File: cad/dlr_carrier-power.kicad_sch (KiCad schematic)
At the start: 17 parts, among them U1 AP2112K-3.3, U2 LP5907MFX-3.8, U9 LMR33630ADDA

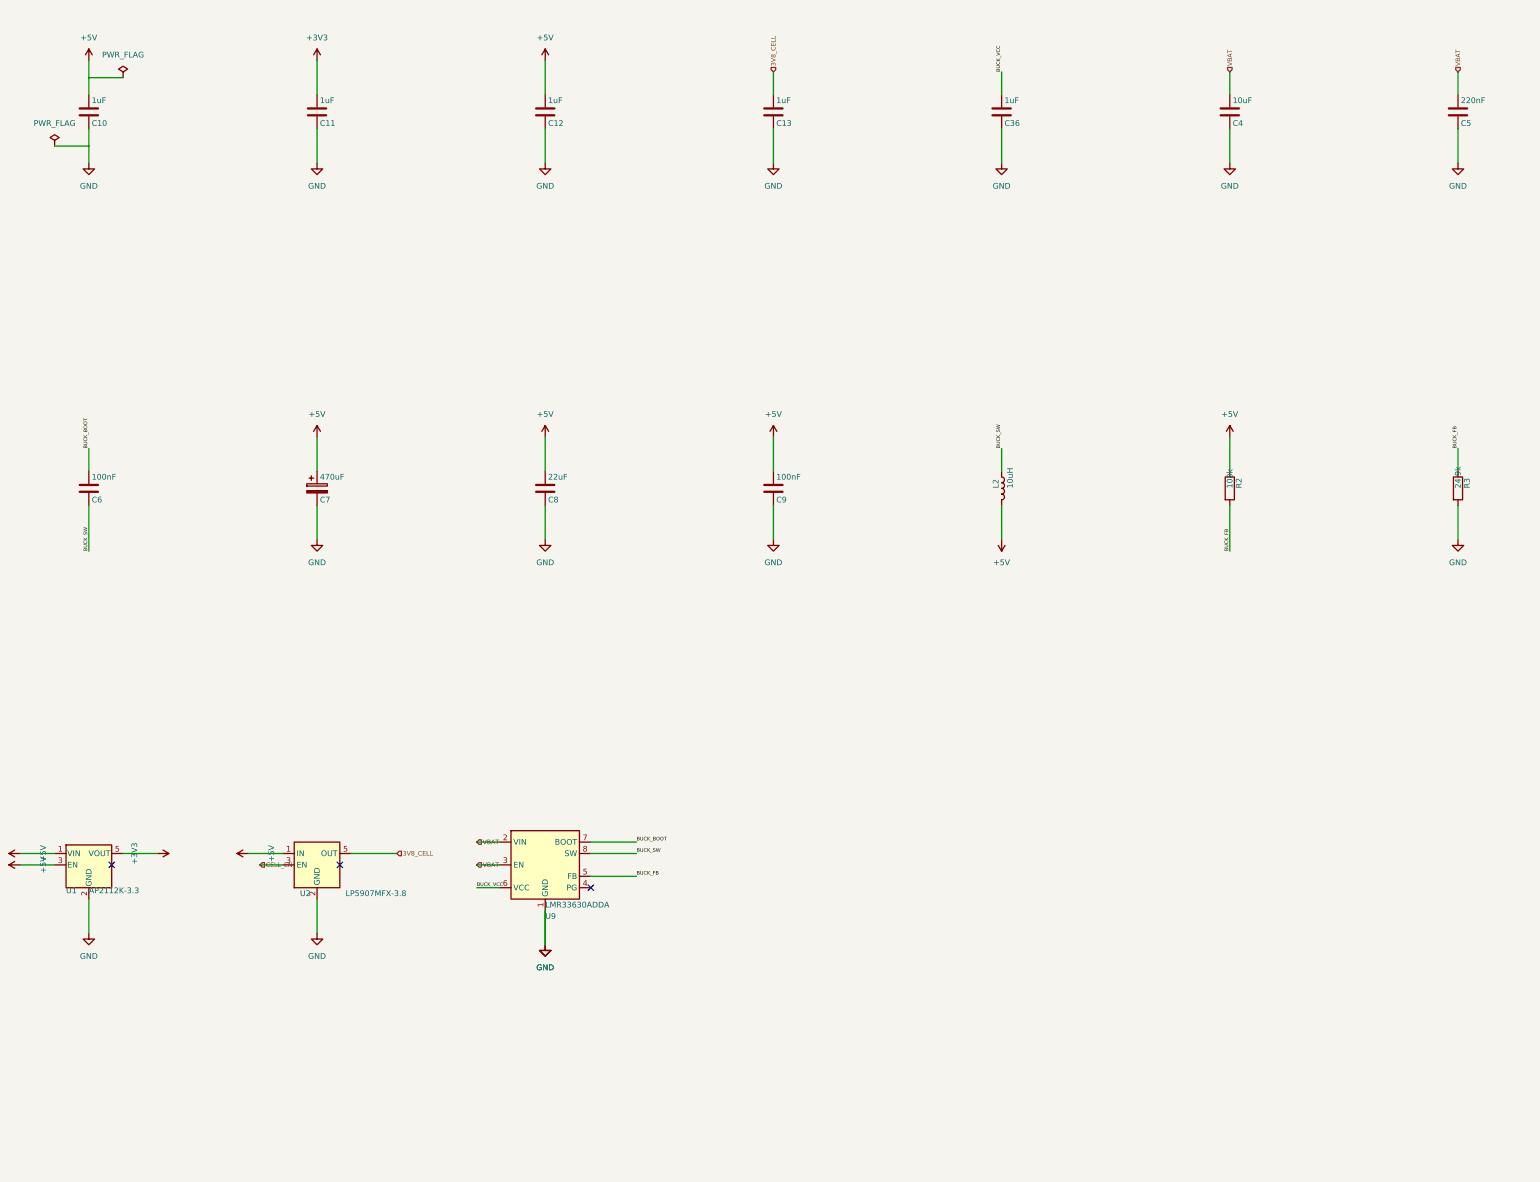
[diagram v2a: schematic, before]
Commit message: 🩺 fix(schematic): match hierarchical label type to the sheet pin
The 117 KiCad 9 errors were a type mismatch, not the hierarchy metadata: every
child hierarchical label was written as `(shape input)` while the root's sheet pins
are bidirectional. KiCad's hier_label_mismatch check compares electrical type as
well as name, so on KiCad 9 every cross-sheet net failed, and the root labels then
read as dangling. KiCad 10 tolerates the mismatch, which is why it passed here.

kicad-sch-api 0.5.6 accepts a shape argument on add_hierarchical_label and ignores
it — the third serialization bug worked around in this generator — so the shape is
rewritten in the saved sheet.

Co-Authored-By: Claude Opus 5 <noreply@anthropic.com>
Claude-Session: https://claude.ai/code/session_011xr7VCL7rkJj2WE2uQF7sF
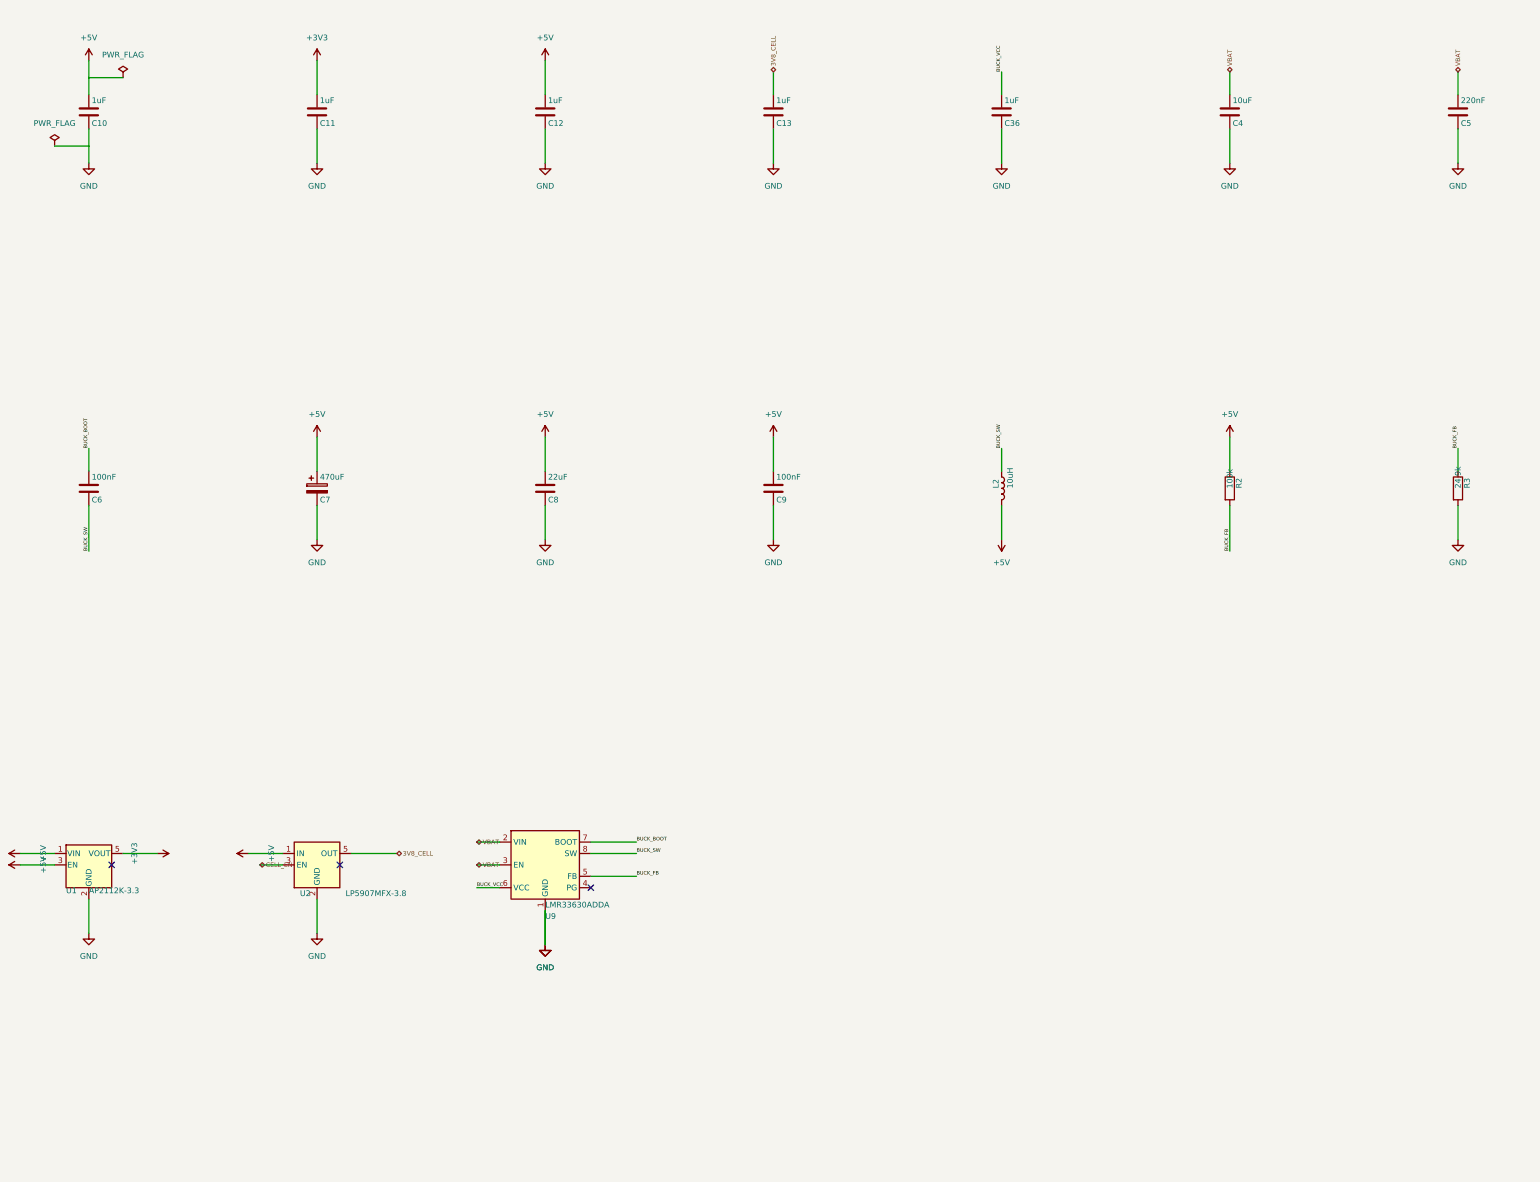
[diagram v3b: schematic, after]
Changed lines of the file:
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@@
 		(instances
 			(project "POWER RAILS"
-				(path "/d7dc1bd5-e6c9-4001-8410-2eaf3fa30cbb"
+				(path "/b92f7d05-346d-4153-84be-6036ac927b56"
 					(reference "C10")
 					(unit 1)
@@
 		(instances
 			(project "POWER RAILS"
-				(path "/d7dc1bd5-e6c9-4001-8410-2eaf3fa30cbb"
+				(path "/b92f7d05-346d-4153-84be-6036ac927b56"
 					(reference "C11")
 					(unit 1)
@@
 		(instances
 			(project "POWER RAILS"
-				(path "/d7dc1bd5-e6c9-4001-8410-2eaf3fa30cbb"
+				(path "/b92f7d05-346d-4153-84be-6036ac927b56"
 					(reference "C12")
 					(unit 1)
@@
 		(instances
 			(project "POWER RAILS"
-				(path "/d7dc1bd5-e6c9-4001-8410-2eaf3fa30cbb"
+				(path "/b92f7d05-346d-4153-84be-6036ac927b56"
 					(reference "C13")
 					(unit 1)
@@
 		(instances
 			(project "POWER RAILS"
-				(path "/d7dc1bd5-e6c9-4001-8410-2eaf3fa30cbb"
+				(path "/b92f7d05-346d-4153-84be-6036ac927b56"
 					(reference "C36")
 					(unit 1)
@@
 		(instances
 			(project "POWER RAILS"
-				(path "/d7dc1bd5-e6c9-4001-8410-2eaf3fa30cbb"
+				(path "/b92f7d05-346d-4153-84be-6036ac927b56"
 					(reference "C4")
 					(unit 1)
@@
 		(instances
 			(project "POWER RAILS"
-				(path "/d7dc1bd5-e6c9-4001-8410-2eaf3fa30cbb"
+				(path "/b92f7d05-346d-4153-84be-6036ac927b56"
 					(reference "C5")
 					(unit 1)
@@
 		(instances
 			(project "POWER RAILS"
-				(path "/d7dc1bd5-e6c9-4001-8410-2eaf3fa30cbb"
+				(path "/b92f7d05-346d-4153-84be-6036ac927b56"
 					(reference "C6")
 					(unit 1)
@@
 		(instances
 			(project "POWER RAILS"
-				(path "/d7dc1bd5-e6c9-4001-8410-2eaf3fa30cbb"
+				(path "/b92f7d05-346d-4153-84be-6036ac927b56"
 					(reference "C7")
 					(unit 1)
@@
 		(instances
 			(project "POWER RAILS"
-				(path "/d7dc1bd5-e6c9-4001-8410-2eaf3fa30cbb"
+				(path "/b92f7d05-346d-4153-84be-6036ac927b56"
 					(reference "C8")
 					(unit 1)
@@
 		(instances
 			(project "POWER RAILS"
-				(path "/d7dc1bd5-e6c9-4001-8410-2eaf3fa30cbb"
+				(path "/b92f7d05-346d-4153-84be-6036ac927b56"
 					(reference "C9")
 					(unit 1)
@@
 		(instances
 			(project "POWER RAILS"
-				(path "/d7dc1bd5-e6c9-4001-8410-2eaf3fa30cbb"
+				(path "/b92f7d05-346d-4153-84be-6036ac927b56"
 					(reference "L2")
 					(unit 1)
@@
 		(instances
 			(project "POWER RAILS"
-				(path "/d7dc1bd5-e6c9-4001-8410-2eaf3fa30cbb"
+				(path "/b92f7d05-346d-4153-84be-6036ac927b56"
 					(reference "R2")
 					(unit 1)
@@
 		(instances
 			(project "POWER RAILS"
-				(path "/d7dc1bd5-e6c9-4001-8410-2eaf3fa30cbb"
+				(path "/b92f7d05-346d-4153-84be-6036ac927b56"
 					(reference "R3")
 					(unit 1)
@@
 		(instances
 			(project "POWER RAILS"
-				(path "/d7dc1bd5-e6c9-4001-8410-2eaf3fa30cbb"
+				(path "/b92f7d05-346d-4153-84be-6036ac927b56"
 					(reference "U1")
 					(unit 1)
@@
 		(instances
 			(project "POWER RAILS"
-				(path "/d7dc1bd5-e6c9-4001-8410-2eaf3fa30cbb"
+				(path "/b92f7d05-346d-4153-84be-6036ac927b56"
 					(reference "U2")
 					(unit 1)
@@
 		(instances
 			(project "POWER RAILS"
-				(path "/d7dc1bd5-e6c9-4001-8410-2eaf3fa30cbb"
+				(path "/b92f7d05-346d-4153-84be-6036ac927b56"
 					(reference "U9")
 					(unit 1)
@@
 		(instances
 			(project "POWER RAILS"
-				(path "/d7dc1bd5-e6c9-4001-8410-2eaf3fa30cbb"
+				(path "/b92f7d05-346d-4153-84be-6036ac927b56"
 					(reference "#PWR001")
 					(unit 1)
@@
 		(instances
 			(project "POWER RAILS"
-				(path "/d7dc1bd5-e6c9-4001-8410-2eaf3fa30cbb"
+				(path "/b92f7d05-346d-4153-84be-6036ac927b56"
 					(reference "#PWR002")
 					(unit 1)
@@
 		(instances
 			(project "POWER RAILS"
-				(path "/d7dc1bd5-e6c9-4001-8410-2eaf3fa30cbb"
+				(path "/b92f7d05-346d-4153-84be-6036ac927b56"
 					(reference "#FLG001")
 					(unit 1)
@@
 		(instances
 			(project "POWER RAILS"
-				(path "/d7dc1bd5-e6c9-4001-8410-2eaf3fa30cbb"
+				(path "/b92f7d05-346d-4153-84be-6036ac927b56"
 					(reference "#PWR003")
 					(unit 1)
@@
 		(instances
 			(project "POWER RAILS"
-				(path "/d7dc1bd5-e6c9-4001-8410-2eaf3fa30cbb"
+				(path "/b92f7d05-346d-4153-84be-6036ac927b56"
 					(reference "#PWR004")
 					(unit 1)
@@
 		(instances
 			(project "POWER RAILS"
-				(path "/d7dc1bd5-e6c9-4001-8410-2eaf3fa30cbb"
+				(path "/b92f7d05-346d-4153-84be-6036ac927b56"
 					(reference "#PWR005")
 					(unit 1)
@@
 		(instances
 			(project "POWER RAILS"
-				(path "/d7dc1bd5-e6c9-4001-8410-2eaf3fa30cbb"
+				(path "/b92f7d05-346d-4153-84be-6036ac927b56"
 					(reference "#PWR006")
 					(unit 1)
@@
 		(instances
 			(project "POWER RAILS"
-				(path "/d7dc1bd5-e6c9-4001-8410-2eaf3fa30cbb"
+				(path "/b92f7d05-346d-4153-84be-6036ac927b56"
 					(reference "#PWR007")
 					(unit 1)
@@
 		(instances
 			(project "POWER RAILS"
-				(path "/d7dc1bd5-e6c9-4001-8410-2eaf3fa30cbb"
+				(path "/b92f7d05-346d-4153-84be-6036ac927b56"
 					(reference "#PWR008")
 					(unit 1)
@@
 		(instances
 			(project "POWER RAILS"
-				(path "/d7dc1bd5-e6c9-4001-8410-2eaf3fa30cbb"
+				(path "/b92f7d05-346d-4153-84be-6036ac927b56"
 					(reference "#PWR009")
 					(unit 1)
@@
 		(instances
 			(project "POWER RAILS"
-				(path "/d7dc1bd5-e6c9-4001-8410-2eaf3fa30cbb"
+				(path "/b92f7d05-346d-4153-84be-6036ac927b56"
 					(reference "#PWR010")
 					(unit 1)
@@
 		(instances
 			(project "POWER RAILS"
-				(path "/d7dc1bd5-e6c9-4001-8410-2eaf3fa30cbb"
+				(path "/b92f7d05-346d-4153-84be-6036ac927b56"
 					(reference "#PWR011")
 					(unit 1)
@@
 		(instances
 			(project "POWER RAILS"
-				(path "/d7dc1bd5-e6c9-4001-8410-2eaf3fa30cbb"
+				(path "/b92f7d05-346d-4153-84be-6036ac927b56"
 					(reference "#PWR012")
 					(unit 1)
@@
 		(instances
 			(project "POWER RAILS"
-				(path "/d7dc1bd5-e6c9-4001-8410-2eaf3fa30cbb"
+				(path "/b92f7d05-346d-4153-84be-6036ac927b56"
 					(reference "#FLG002")
 					(unit 1)
@@
 		(instances
 			(project "POWER RAILS"
-				(path "/d7dc1bd5-e6c9-4001-8410-2eaf3fa30cbb"
+				(path "/b92f7d05-346d-4153-84be-6036ac927b56"
 					(reference "#PWR013")
 					(unit 1)
@@
 		(instances
 			(project "POWER RAILS"
-				(path "/d7dc1bd5-e6c9-4001-8410-2eaf3fa30cbb"
+				(path "/b92f7d05-346d-4153-84be-6036ac927b56"
 					(reference "#PWR014")
 					(unit 1)
@@
 		(instances
 			(project "POWER RAILS"
-				(path "/d7dc1bd5-e6c9-4001-8410-2eaf3fa30cbb"
+				(path "/b92f7d05-346d-4153-84be-6036ac927b56"
 					(reference "#PWR015")
 					(unit 1)
@@
 		(instances
 			(project "POWER RAILS"
-				(path "/d7dc1bd5-e6c9-4001-8410-2eaf3fa30cbb"
+				(path "/b92f7d05-346d-4153-84be-6036ac927b56"
 					(reference "#PWR016")
 					(unit 1)
@@
 		(instances
 			(project "POWER RAILS"
-				(path "/d7dc1bd5-e6c9-4001-8410-2eaf3fa30cbb"
+				(path "/b92f7d05-346d-4153-84be-6036ac927b56"
 					(reference "#PWR017")
 					(unit 1)
@@
 		(instances
 			(project "POWER RAILS"
-				(path "/d7dc1bd5-e6c9-4001-8410-2eaf3fa30cbb"
+				(path "/b92f7d05-346d-4153-84be-6036ac927b56"
 					(reference "#PWR018")
 					(unit 1)
@@
 		(instances
 			(project "POWER RAILS"
-				(path "/d7dc1bd5-e6c9-4001-8410-2eaf3fa30cbb"
+				(path "/b92f7d05-346d-4153-84be-6036ac927b56"
 					(reference "#PWR019")
 					(unit 1)
@@
 		(instances
 			(project "POWER RAILS"
-				(path "/d7dc1bd5-e6c9-4001-8410-2eaf3fa30cbb"
+				(path "/b92f7d05-346d-4153-84be-6036ac927b56"
 					(reference "#PWR020")
 					(unit 1)
@@
 		(instances
 			(project "POWER RAILS"
-				(path "/d7dc1bd5-e6c9-4001-8410-2eaf3fa30cbb"
+				(path "/b92f7d05-346d-4153-84be-6036ac927b56"
 					(reference "#PWR021")
 					(unit 1)
@@
 		(instances
 			(project "POWER RAILS"
-				(path "/d7dc1bd5-e6c9-4001-8410-2eaf3fa30cbb"
+				(path "/b92f7d05-346d-4153-84be-6036ac927b56"
 					(reference "#PWR022")
 					(unit 1)
@@
 		(instances
 			(project "POWER RAILS"
-				(path "/d7dc1bd5-e6c9-4001-8410-2eaf3fa30cbb"
+				(path "/b92f7d05-346d-4153-84be-6036ac927b56"
 					(reference "#PWR023")
 					(unit 1)
@@
 		(instances
 			(project "POWER RAILS"
-				(path "/d7dc1bd5-e6c9-4001-8410-2eaf3fa30cbb"
+				(path "/b92f7d05-346d-4153-84be-6036ac927b56"
 					(reference "#PWR024")
 					(unit 1)
@@
 		(instances
 			(project "POWER RAILS"
-				(path "/d7dc1bd5-e6c9-4001-8410-2eaf3fa30cbb"
+				(path "/b92f7d05-346d-4153-84be-6036ac927b56"
 					(reference "#PWR025")
 					(unit 1)
@@
 		(instances
 			(project "POWER RAILS"
-				(path "/d7dc1bd5-e6c9-4001-8410-2eaf3fa30cbb"
+				(path "/b92f7d05-346d-4153-84be-6036ac927b56"
 					(reference "#PWR026")
 					(unit 1)
@@
 		(instances
 			(project "POWER RAILS"
-				(path "/d7dc1bd5-e6c9-4001-8410-2eaf3fa30cbb"
+				(path "/b92f7d05-346d-4153-84be-6036ac927b56"
 					(reference "#PWR027")
 					(unit 1)
@@
 	)
 	(hierarchical_label "3V8_CELL"
-		(shape input)
+		(shape bidirectional)
 		(at 215.9 71.12 90)
 		(effects
@@
 	)
 	(hierarchical_label "3V8_CELL"
-		(shape input)
+		(shape bidirectional)
 		(at 132.08 245.11 0)
 		(effects
@@
 	)
 	(hierarchical_label "CELL_EN"
-		(shape input)
+		(shape bidirectional)
 		(at 101.6 247.65 180)
 		(effects
@@
 	)
 	(hierarchical_label "VBAT"
-		(shape input)
+		(shape bidirectional)
 		(at 317.5 71.12 90)
 		(effects
@@
 	)
 	(hierarchical_label "VBAT"
-		(shape input)
+		(shape bidirectional)
 		(at 368.3 71.12 90)
 		(effects
@@
 	)
 	(hierarchical_label "VBAT"
-		(shape input)
+		(shape bidirectional)
 		(at 149.86 242.57 180)
 		(effects
@@
 	)
 	(hierarchical_label "VBAT"
-		(shape input)
+		(shape bidirectional)
 		(at 149.86 247.65 180)
 		(effects
@@
 	)
 	(sheet_instances
-		(path "/97c4eb20-bf89-4022-8442-9e89007a385b"
+		(path "/c5c169f4-6c30-478e-8391-6862f9d11774"
 			(page "3")
 		)
